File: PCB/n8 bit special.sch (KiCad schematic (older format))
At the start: 9 parts, among them U1 W65C02SxP, U2 CY62256-70PC, U3 28C256

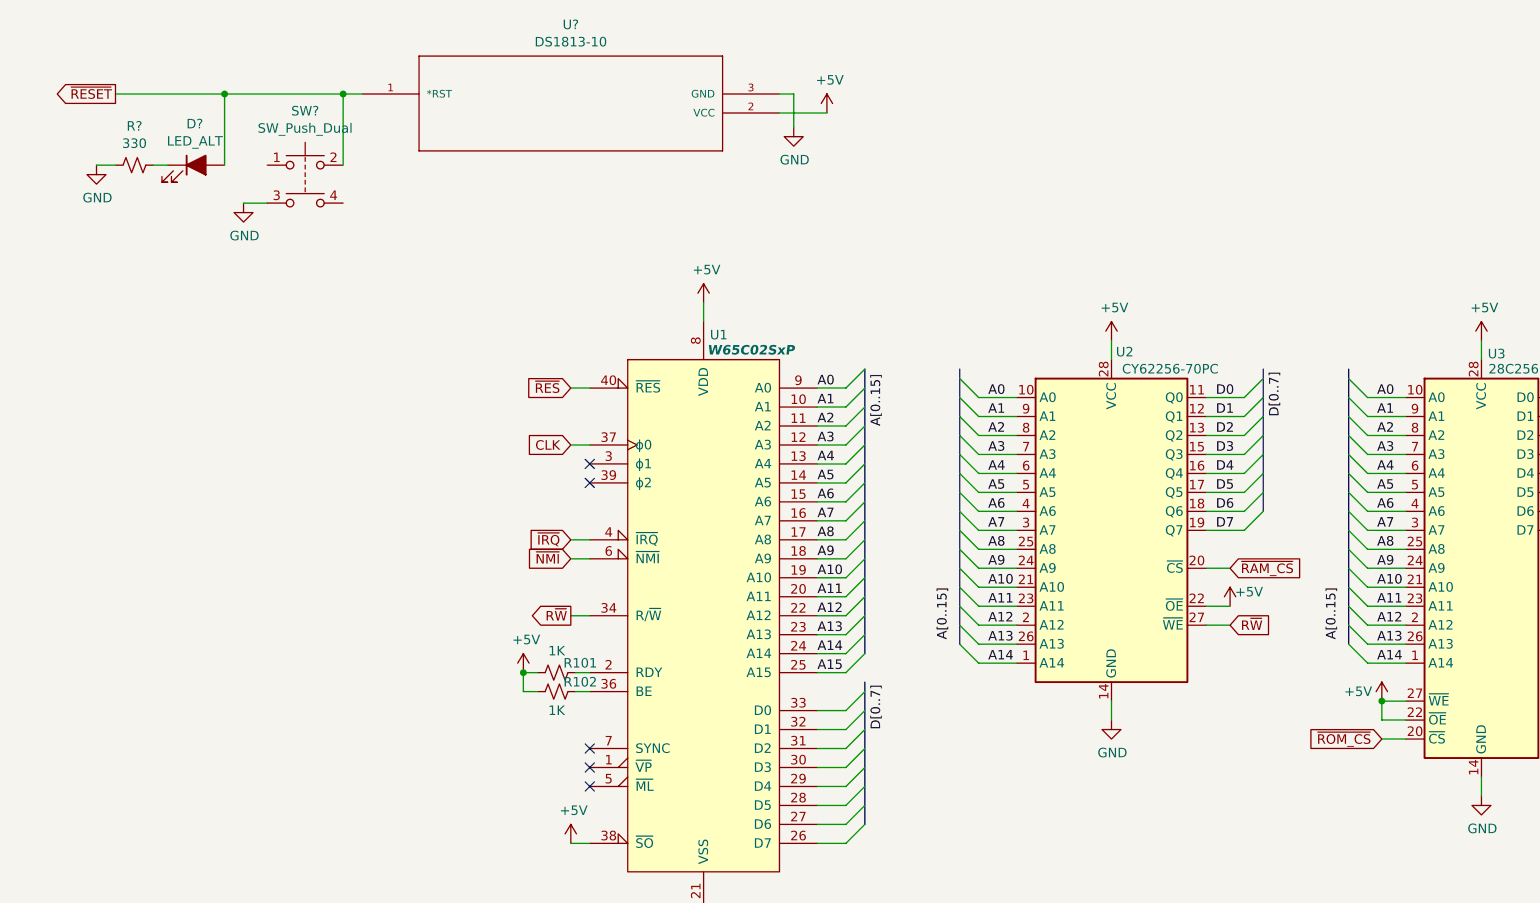
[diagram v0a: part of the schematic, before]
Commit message: Fixed some issues with output enable connections
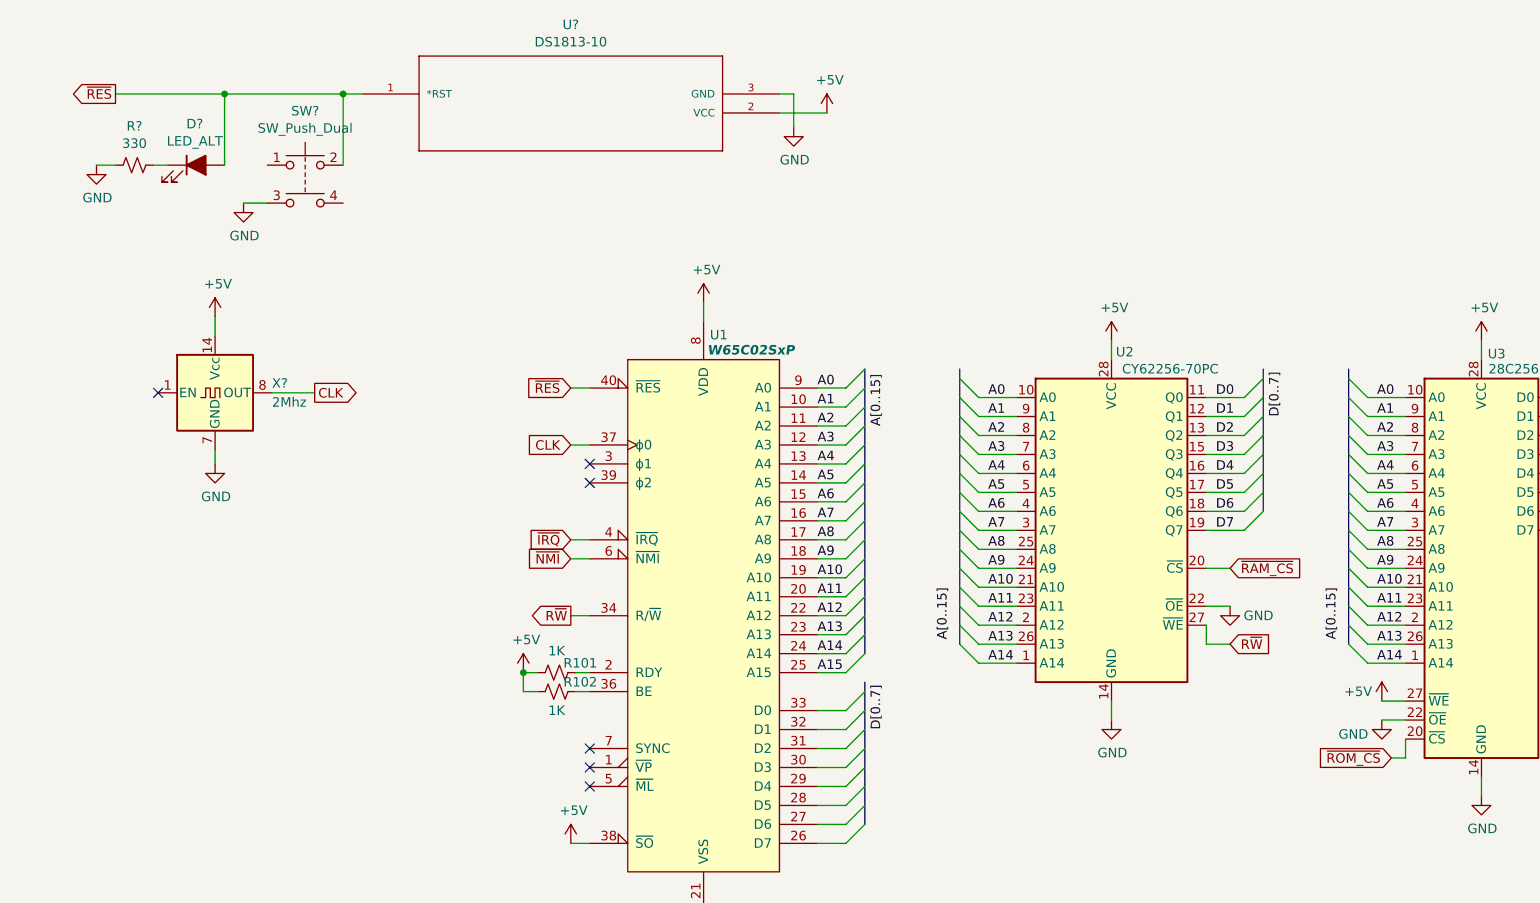
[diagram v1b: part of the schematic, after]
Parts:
- added X?: 2Mhz, Oscillator:Oscillator_DIP-14, symbol Oscillator:CXO_DIP14
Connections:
- net ~RESET is gone; now on net ~RES: D?.2 (A), SW?.2, U?.1 (*RST)
- net +5V: now also X?.14 (Vcc); no longer U2.22 (~OE), U3.22 (~OE)
- net CLK: now also X?.8 (OUT)
- net GND: now also U2.22 (~OE), U3.22 (~OE), X?.7 (GND)
- no-connect marks 5 -> 6
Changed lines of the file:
@@
 Text GLabel 6825 3450 2    50   Input ~ 0
 ~RAM_CS
-$Comp
-L power:+5V #PWR0110
-U 1 1 604E7AE4
-P 6825 3650
-F 0 "#PWR0110" H 6825 3500 50  0001 C CNN
-F 1 "+5V" H 6925 3725 50  0000 C CNN
-F 2 "" H 6825 3650 50  0001 C CNN
-F 3 "" H 6825 3650 50  0001 C CNN
-	1    6825 3650
-	1    0    0    -1
-$EndComp
 Wire Wire Line
 	6700 3450 6825 3450
 Wire Wire Line
 	6700 3650 6825 3650
-Wire Wire Line
-	7750 4250 7625 4250
-Wire Wire Line
-	7625 4250 7625 4150
-Connection ~ 7625 4150
-Text GLabel 7625 4350 0    50   Input ~ 0
-~ROM_CS
-Wire Wire Line
-	7750 4350 7625 4350
-Text GLabel 6825 3750 2    50   Input ~ 0
+Text GLabel 6825 3850 2    50   Input ~ 0
 R~W
-Wire Wire Line
-	6700 3750 6825 3750
 Wire Wire Line
 	950  1325 850  1325
@@
 $EndComp
 Text GLabel 950  950  0    50   Output ~ 0
-~RESET
+~RES
 $Comp
 L DS1813-10:DS1813-10 U?
@@
 	1    0    0    -1
 $EndComp
+$Comp
+L power:GND #PWR?
+U 1 1 60420A5A
+P 1475 2900
+F 0 "#PWR?" H 1475 2650 50  0001 C CNN
+F 1 "GND" H 1480 2727 50  0000 C CNN
+F 2 "" H 1475 2900 50  0001 C CNN
+F 3 "" H 1475 2900 50  0001 C CNN
+	1    1475 2900
+	1    0    0    -1
+$EndComp
+$Comp
+L power:+5V #PWR?
+U 1 1 604216C0
+P 1475 2125
+F 0 "#PWR?" H 1475 1975 50  0001 C CNN
+F 1 "+5V" H 1490 2298 50  0000 C CNN
+F 2 "" H 1475 2125 50  0001 C CNN
+F 3 "" H 1475 2125 50  0001 C CNN
+	1    1475 2125
+	1    0    0    -1
+$EndComp
+Wire Wire Line
+	1475 2125 1475 2225
+Wire Wire Line
+	1475 2825 1475 2900
+NoConn ~ 1175 2525
+Text GLabel 2000 2525 2    50   Output ~ 0
+CLK
+Wire Wire Line
+	1775 2525 2000 2525
+$Comp
+L Oscillator:CXO_DIP14 X?
+U 1 1 6041F292
+P 1475 2525
+F 0 "X?" H 1775 2575 50  0000 L CNN
+F 1 "2Mhz" H 1775 2475 50  0000 L CNN
+F 2 "Oscillator:Oscillator_DIP-14" H 1925 2175 50  0001 C CNN
+F 3 "http://cdn-reichelt.de/documents/datenblatt/B400/OSZI.pdf" H 1375 2525 50  0001 C CNN
+	1    1475 2525
+	1    0    0    -1
+$EndComp
+$Comp
+L power:GND #PWR?
+U 1 1 6046D622
+P 7625 4250
+F 0 "#PWR?" H 7625 4000 50  0001 C CNN
+F 1 "GND" H 7475 4175 50  0000 C CNN
+F 2 "" H 7625 4250 50  0001 C CNN
+F 3 "" H 7625 4250 50  0001 C CNN
+	1    7625 4250
+	1    0    0    -1
+$EndComp
+Wire Wire Line
+	7750 4250 7625 4250
+Wire Wire Line
+	7750 4350 7750 4450
+Wire Wire Line
+	7750 4450 7675 4450
+Text GLabel 7675 4450 0    50   Input ~ 0
+~ROM_CS
+$Comp
+L power:GND #PWR?
+U 1 1 604ADFAE
+P 6825 3650
+F 0 "#PWR?" H 6825 3400 50  0001 C CNN
+F 1 "GND" H 6975 3600 50  0000 C CNN
+F 2 "" H 6825 3650 50  0001 C CNN
+F 3 "" H 6825 3650 50  0001 C CNN
+	1    6825 3650
+	1    0    0    -1
+$EndComp
+Wire Wire Line
+	6700 3750 6700 3850
+Wire Wire Line
+	6700 3850 6825 3850
 Wire Bus Line
 	8850 2400 8850 3150

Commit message: Start of PCB layout
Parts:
- added C1, C10, C11, C12, C13, C14, C15, C3, C4, C5, C6, C7, C8, C9: 100nf, Capacitor_THT:C_Disc_D5.0mm_W2.5mm_P2.50mm, symbol Device:C_Small
- added C2: 1000uF, Capacitor_THT:CP_Radial_D10.0mm_P5.00mm, symbol Device:CP
- added J1: PowerPort, Connector_PinSocket_2.54mm:PinSocket_1x04_P2.54mm_Vertical, symbol Connector_Generic:Conn_01x04
- added J2: PORT0, Connector_PinSocket_2.54mm:PinSocket_2x16_P2.54mm_Vertical, symbol Connector_Generic:Conn_02x16_Odd_Even
- added J3: PORT2, Connector_PinSocket_2.54mm:PinSocket_2x16_P2.54mm_Vertical, symbol Connector_Generic:Conn_02x16_Odd_Even
- added J4: PORT1, Connector_PinSocket_2.54mm:PinSocket_2x16_P2.54mm_Vertical, symbol Connector_Generic:Conn_02x16_Odd_Even
- added J5: PORT3, Connector_PinSocket_2.54mm:PinSocket_2x16_P2.54mm_Vertical, symbol Connector_Generic:Conn_02x16_Odd_Even
- added J6: Conn_02x08_Odd_Even, Connector_PinHeader_2.54mm:PinHeader_2x08_P2.54mm_Vertical, symbol Connector_Generic:Conn_02x08_Odd_Even
- added RN1: 3K3, Resistor_THT:R_Array_SIP9, symbol Device:R_Network08
- added U3: CY62256-70PC, Package_DIP:DIP-28_W15.24mm, symbol Memory_RAM:CY62256-70PC
- added U5: 74LS21, Package_DIP:DIP-12_W7.62mm, symbol 74xx:74LS21
- added U6: 22V10C, Package_DIP:DIP-24_W7.62mm_Socket, symbol 6502:22V10C
- D1: renamed from D?; footprint (none) -> LED_THT:LED_D3.0mm
- R1: renamed from R?; footprint (none) -> Resistor_THT:R_Axial_DIN0207_L6.3mm_D2.5mm_P7.62mm_Horizontal; symbol Device:R_Small_US -> Device:R
- R2: renamed from R101; value 1K -> 3K3; footprint (none) -> Resistor_THT:R_Axial_DIN0207_L6.3mm_D2.5mm_P7.62mm_Horizontal; symbol Device:R_Small_US -> Device:R
- R3: renamed from R102; value 1K -> 3K3; footprint (none) -> Resistor_THT:R_Axial_DIN0207_L6.3mm_D2.5mm_P7.62mm_Horizontal; symbol Device:R_Small_US -> Device:R
- SW1: renamed from SW?; footprint Button_Switch_THT:SW_PUSH-12mm -> Button_Switch_THT:SW_PUSH_6mm; symbol Switch:SW_Push_Dual -> Switch:SW_Push_Dual_x2
- U7: renamed from U?; value DS1813-10 -> DS1813; footprint (none) -> Package_TO_SOT_THT:TO-92; symbol DS1813-10:DS1813-10 -> 6502:DS1813
- gave numbers to parts that had none: 1
- renumbered U3 to U4
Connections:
- net +5V: now also C1.2, C10.1, C11.1, C12.1, C13.1, C14.1, C15.2, C2.1, C3.2, C4.1, C5.2, C6.1, C7.2, C8.1, C9.2, J1.1 (Pin_1), J2.1 (Pin_1), J2.2 (Pin_2), J2.29 (Pin_29), J2.30 (Pin_30), J3.1 (Pin_1), J3.2 (Pin_2), J3.29 (Pin_29), J3.30 (Pin_30), J4.1 (Pin_1), J4.2 (Pin_2), J4.29 (Pin_29), J4.30 (Pin_30), J5.1 (Pin_1), J5.2 (Pin_2), J5.29 (Pin_29), J5.30 (Pin_30), RN1.1 (common), U3.28 (VCC), U5.14 (VCC), U6.24 (VCC)
- net A0: now also J2.5 (Pin_5), J3.5 (Pin_5), J4.5 (Pin_5), J5.5 (Pin_5), U3.10 (A0)
- net A1: now also J2.7 (Pin_7), J3.7 (Pin_7), J4.7 (Pin_7), J5.7 (Pin_7), U3.9 (A1)
- net A10: now also U3.21 (A10), U6.6 (IN6)
- net A11: now also U3.23 (A11), U6.7 (IN7)
- net A12: now also U3.2 (A12), U6.8 (IN8)
- net A13: now also U3.26 (A13), U6.9 (IN9)
- net A14: now also U3.1 (A14), U6.10 (IN10)
- net A15: now also U6.11 (IN11)
- net A2: now also J2.9 (Pin_9), J3.9 (Pin_9), J4.9 (Pin_9), J5.9 (Pin_9), U3.8 (A2)
- net A3: now also J2.11 (Pin_11), J3.11 (Pin_11), J4.11 (Pin_11), J5.11 (Pin_11), U3.7 (A3)
- net A4: now also J2.13 (Pin_13), J3.13 (Pin_13), J4.13 (Pin_13), J5.13 (Pin_13), U3.6 (A4)
- net A5: now also J2.15 (Pin_15), J3.15 (Pin_15), J4.15 (Pin_15), J5.15 (Pin_15), U3.5 (A5)
- net A6: now also U3.4 (A6), U6.2 (IN2)
- net A7: now also U3.3 (A7), U6.3 (IN3)
- net A8: now also U3.25 (A8), U6.4 (IN4/PD)
- net A9: now also U3.24 (A9), U6.5 (IN5)
- net CLK: now also J2.21 (Pin_21), J3.21 (Pin_21), J4.21 (Pin_21), J5.21 (Pin_21), U6.1 (CLK/IN1)
- net D0: now also U1.33 (D0), J2.6 (Pin_6), J3.6 (Pin_6), J4.6 (Pin_6), J5.6 (Pin_6), U3.11 (Q0)
- net D1: now also U1.32 (D1), J2.8 (Pin_8), J3.8 (Pin_8), J4.8 (Pin_8), J5.8 (Pin_8), U3.12 (Q1)
- net D2: now also U1.31 (D2), J2.10 (Pin_10), J3.10 (Pin_10), J4.10 (Pin_10), J5.10 (Pin_10), U3.13 (Q2)
- net D3: now also U1.30 (D3), J2.12 (Pin_12), J3.12 (Pin_12), J4.12 (Pin_12), J5.12 (Pin_12), U3.15 (Q3)
- net D4: now also U1.29 (D4), J2.14 (Pin_14), J3.14 (Pin_14), J4.14 (Pin_14), J5.14 (Pin_14), U3.16 (Q4)
- net D5: now also U1.28 (D5), J2.16 (Pin_16), J3.16 (Pin_16), J4.16 (Pin_16), J5.16 (Pin_16), U3.17 (Q5)
- net D6: now also U1.27 (D6), J2.18 (Pin_18), J3.18 (Pin_18), J4.18 (Pin_18), J5.18 (Pin_18), U3.18 (Q6)
- net D7: now also U1.26 (D7), J2.20 (Pin_20), J3.20 (Pin_20), J4.20 (Pin_20), J5.20 (Pin_20), U3.19 (Q7)
- net GND: now also SW1.2 (D), C1.1, C10.2, C11.2, C12.2, C13.2, C14.2, C15.1, C2.2, C3.1, C4.2, C5.1, C6.2, C7.1, C8.2, C9.1, J1.4 (Pin_4), J2.3 (Pin_3), J2.31 (Pin_31), J2.32 (Pin_32), J2.4 (Pin_4), J3.3 (Pin_3), J3.31 (Pin_31), J3.32 (Pin_32), J3.4 (Pin_4), J4.3 (Pin_3), J4.31 (Pin_31), J4.32 (Pin_32), J4.4 (Pin_4), J5.3 (Pin_3), J5.31 (Pin_31), J5.32 (Pin_32), J5.4 (Pin_4), U3.14 (GND), U3.22 (~OE), U5.7 (GND), U6.12 (GND); no longer SW1.3
- net R~W: now also J2.19 (Pin_19), J3.19 (Pin_19), J4.19 (Pin_19), J5.19 (Pin_19), U3.27 (~WE), U6.13 (IN12)
- net ~IRQ: now also U5.6
- net ~NMI: now also U5.8
- net ~RES: now also SW1.1 (C), J2.23 (Pin_23), J3.23 (Pin_23), J4.23 (Pin_23), J5.23 (Pin_23); no longer SW1.2
- net ~ROM_CS: now also U6.23 (IO22)
- net ~RAM_CS renamed ~RAM1_CS
- net ~RAM1_CS: now also U6.22 (IO21)
- new net: J6.2 (Pin_2), RN1.2 (R1)
- new net: J6.4 (Pin_4), RN1.3 (R2)
- new net: J6.6 (Pin_6), RN1.4 (R3)
- new net: J6.8 (Pin_8), RN1.5 (R4)
- new net: J6.10 (Pin_10), RN1.6 (R5)
- new net: J6.12 (Pin_12), RN1.7 (R6)
- new net: J6.14 (Pin_14), RN1.8 (R7)
- new net: J6.16 (Pin_16), RN1.9 (R8)
- new net FUTURE0: J2.25 (Pin_25), J3.25 (Pin_25), J4.25 (Pin_25), J5.25 (Pin_25), U6.16 (IO15)
- new net FUTURE1: J2.27 (Pin_27), J3.27 (Pin_27), J4.27 (Pin_27), J5.27 (Pin_27), U6.15 (IO14)
- new net PORT0_IRQ_PULLUP: J2.22 (Pin_22), J6.1 (Pin_1), U5.1
- new net PORT0_NMI_PULLUP: J2.24 (Pin_24), J6.3 (Pin_3), U5.9
- new net PORT1_IRQ_PULLUP: J4.22 (Pin_22), J6.5 (Pin_5), U5.2
- new net PORT1_NMI_PULLUP: J4.24 (Pin_24), J6.7 (Pin_7), U5.10
- new net PORT2_IRQ_PULLUP: J3.22 (Pin_22), J6.9 (Pin_9), U5.4
- new net PORT2_NMI_PULLUP: J3.24 (Pin_24), J6.11 (Pin_11), U5.12
- new net PORT3_IRQ_PULLUP: J5.22 (Pin_22), J6.13 (Pin_13), U5.5
- new net PORT3_NMI_PULLUP: J5.24 (Pin_24), J6.15 (Pin_15), U5.13
- new net USB_D+: J1.2 (Pin_2), J2.26 (Pin_26), J3.26 (Pin_26), J4.26 (Pin_26), J5.26 (Pin_26)
- new net USB_D-: J1.3 (Pin_3), J2.28 (Pin_28), J3.28 (Pin_28), J4.28 (Pin_28), J5.28 (Pin_28)
- new net ~PORT0_CS: J2.17 (Pin_17), U6.20 (IO19)
- new net ~PORT1_CS: J4.17 (Pin_17), U6.19 (IO18)
- new net ~PORT2_CS: J3.17 (Pin_17), U6.18 (IO17)
- new net ~PORT3_CS: J5.17 (Pin_17), U6.17 (IO16)
- new net ~RAM2_CS: U3.20 (~CS), U6.21 (IO20)
- no-connect marks 6 -> 7
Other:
- note added: "CPU"
- note added: "Device Interrupts"
- note added: "Expansion Ports"
- note added: "Glue Logic"
- note added: "Memory"
- note added: "Power\n"
- note added: "Reset\n"
- note added: "System Clock"
- moved on the sheet: D1, U1, U2, U4, X1

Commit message: Near final board
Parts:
- U1: footprint Package_DIP:DIP-40_W15.24mm -> Package_DIP:DIP-40_W15.24mm_Socket
- U2, U3, U4: footprint Package_DIP:DIP-28_W15.24mm -> Package_DIP:DIP-28_W15.24mm_Socket
- U5: footprint Package_DIP:DIP-12_W7.62mm -> Package_DIP:DIP-14_W7.62mm_Socket
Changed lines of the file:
@@
 F 0 "U2" H 9570 3190 50  0000 C CNN
 F 1 "CY62256-70PC" H 9810 3100 50  0000 C CNN
-F 2 "Package_DIP:DIP-28_W15.24mm" H 9500 2150 50  0001 C CNN
+F 2 "Package_DIP:DIP-28_W15.24mm_Socket" H 9500 2150 50  0001 C CNN
 F 3 "https://ecee.colorado.edu/~mcclurel/Cypress_SRAM_CY62256.pdf" H 9500 2150 50  0001 C CNN
 	1    9500 2250
@@
 F 0 "U1" H 6930 4305 50  0000 C CNN
 F 1 "W65C02SxP" H 7100 4225 50  0000 C CNN
-F 2 "Package_DIP:DIP-40_W15.24mm" H 6850 4825 50  0001 C CNN
+F 2 "Package_DIP:DIP-40_W15.24mm_Socket" H 6850 4825 50  0001 C CNN
 F 3 "http://www.westerndesigncenter.com/wdc/documentation/w65c02s.pdf" H 6850 4725 50  0001 C CNN
 	1    6850 2825
@@
 F 0 "U5" H 1650 6100 50  0000 C CNN
 F 1 "74LS21" H 1650 6009 50  0000 C CNN
-F 2 "Package_DIP:DIP-12_W7.62mm" H 1650 5725 50  0001 C CNN
+F 2 "Package_DIP:DIP-14_W7.62mm_Socket" H 1650 5725 50  0001 C CNN
 F 3 "http://www.ti.com/lit/gpn/sn74LS21" H 1650 5725 50  0001 C CNN
 	1    1650 5725
@@
 F 0 "U5" H 1650 6800 50  0000 C CNN
 F 1 "74LS21" H 1650 6709 50  0000 C CNN
-F 2 "Package_DIP:DIP-12_W7.62mm" H 1650 6425 50  0001 C CNN
+F 2 "Package_DIP:DIP-14_W7.62mm_Socket" H 1650 6425 50  0001 C CNN
 F 3 "http://www.ti.com/lit/gpn/sn74LS21" H 1650 6425 50  0001 C CNN
 	2    1650 6425
@@
 F 0 "U3" H 12045 3190 50  0000 C CNN
 F 1 "CY62256-70PC" H 12285 3100 50  0000 C CNN
-F 2 "Package_DIP:DIP-28_W15.24mm" H 11975 2150 50  0001 C CNN
+F 2 "Package_DIP:DIP-28_W15.24mm_Socket" H 11975 2150 50  0001 C CNN
 F 3 "https://ecee.colorado.edu/~mcclurel/Cypress_SRAM_CY62256.pdf" H 11975 2150 50  0001 C CNN
 	1    11975 2250
@@
 F 0 "U4" H 14405 3555 50  0000 C CNN
 F 1 "28C256" H 14495 3475 50  0000 C CNN
-F 2 "Package_DIP:DIP-28_W15.24mm" H 14325 2425 50  0001 C CNN
+F 2 "Package_DIP:DIP-28_W15.24mm_Socket" H 14325 2425 50  0001 C CNN
 F 3 "http://ww1.microchip.com/downloads/en/DeviceDoc/doc0006.pdf" H 14325 2425 50  0001 C CNN
 	1    14325 2425
@@
 F 0 "U5" H 1855 7521 50  0000 L CNN
 F 1 "74LS21" H 1855 7430 50  0000 L CNN
-F 2 "Package_DIP:DIP-12_W7.62mm" H 1625 7475 50  0001 C CNN
+F 2 "Package_DIP:DIP-14_W7.62mm_Socket" H 1625 7475 50  0001 C CNN
 F 3 "http://www.ti.com/lit/gpn/sn74LS21" H 1625 7475 50  0001 C CNN
 	3    1625 7475
@@
 Wire Wire Line
 	2875 4500 3325 4500
+Connection ~ 3325 4500
+$Comp
+L Device:R R2
+U 1 1 6047D0F1
+P 6025 3125
+F 0 "R2" V 5925 3125 50  0000 C CNN
+F 1 "3K3" V 6025 3125 50  0000 C CNN
+F 2 "Resistor_THT:R_Axial_DIN0207_L6.3mm_D2.5mm_P7.62mm_Horizontal" H 6025 3125 50  0001 C CNN
+F 3 "~" H 6025 3125 50  0001 C CNN
+	1    6025 3125
+	0    1    1    0
+$EndComp
 Wire Bus Line
 	6375 8950 6375 9450
@@
 Wire Bus Line
 	13625 1425 13625 2825
-Connection ~ 3325 4500
-$Comp
-L Device:R R2
-U 1 1 6047D0F1
-P 6025 3125
-F 0 "R2" V 5925 3125 50  0000 C CNN
-F 1 "3K3" V 6025 3125 50  0000 C CNN
-F 2 "Resistor_THT:R_Axial_DIN0207_L6.3mm_D2.5mm_P7.62mm_Horizontal" H 6025 3125 50  0001 C CNN
-F 3 "~" H 6025 3125 50  0001 C CNN
-	1    6025 3125
-	0    1    1    0
-$EndComp
 $EndSCHEMATC

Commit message: Added production gerbers
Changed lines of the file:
@@
 Wire Bus Line
 	13625 1425 13625 2825
+Text Label 8650 2825 1    50   ~ 0
+A[0..15]
 $EndSCHEMATC
